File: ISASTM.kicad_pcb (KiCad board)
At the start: 4 copper layers, 101.6 x 101.6 mm, 137 parts, among them J1 Bus_ISA_8bit, J2 USB_C_Receptacle_USB2.0, J3 Boot select, J4 USB_C_Receptacle_USB2.0, J5 TagConnect_TC2030_SWD, SW1 Reset, U1 STM32H743IITx, U10 SN74AVC8T245PW, U11 SN74AVC8T245PW, U12 SN74AVC8T245PW, U13 SN74AVC8T245PW, U14 SRV05-4, U15 USB3343, U2 MT48LC16M16A2P, U3 SN74AVC8T245PW, U4 SN74AVC8T245PW, U5 AMS1117-3.3, U6 SN74AVC8T245PW, U7 SN74AVC8T245PW, U8 SN74AVC8T245PW, U9 SN74AVC8T245PW, X1 SG-7050CAN, Y1 26 MHz, Y2 8 MHz

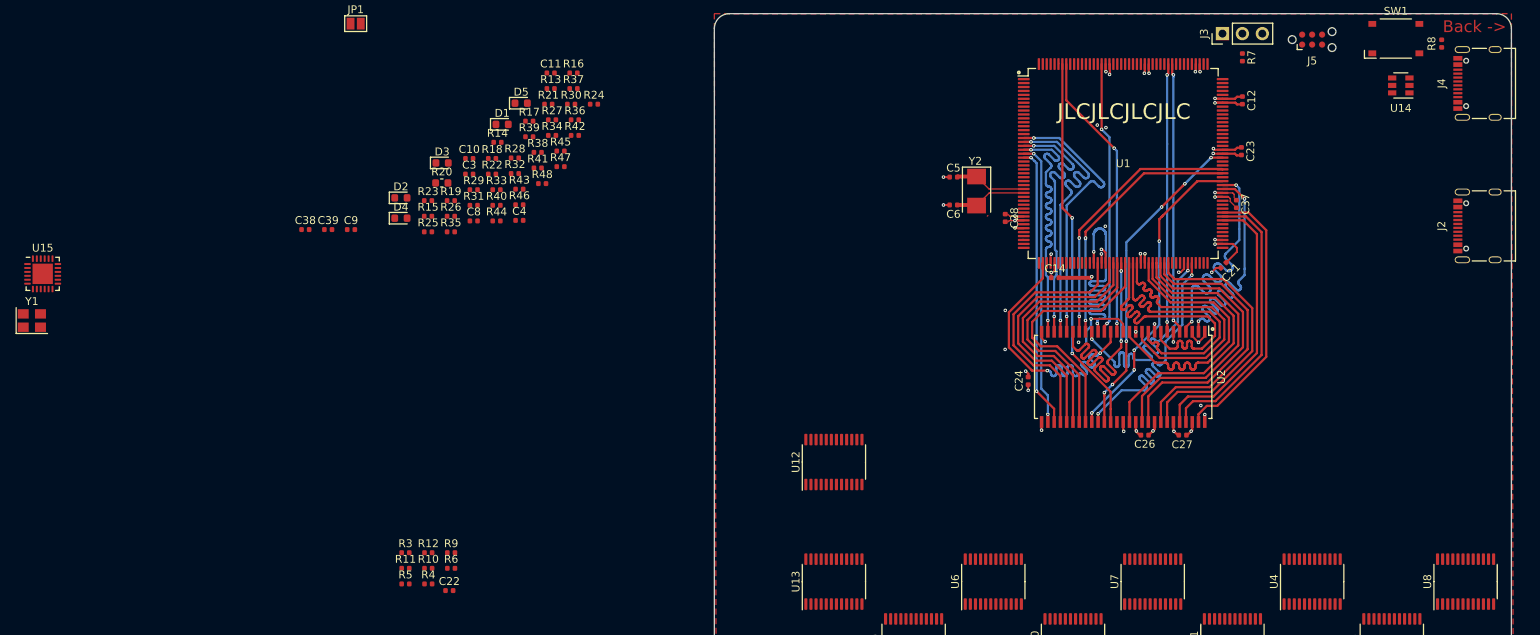
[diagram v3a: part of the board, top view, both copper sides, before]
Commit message: Finish fanout and ULPI routing
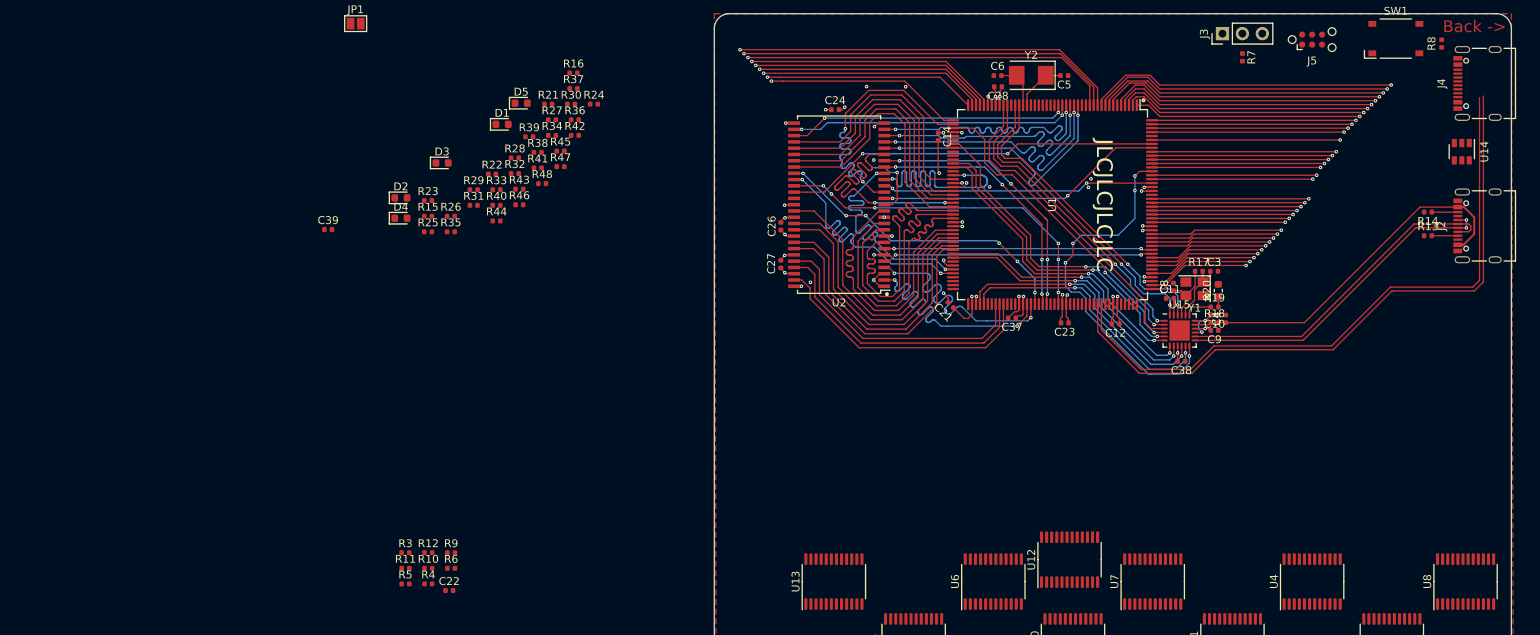
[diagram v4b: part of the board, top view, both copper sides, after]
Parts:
- moved Y1 148.3 mm to (76.5, 49.7), turned to 180 degrees
- moved U15 145.1 mm to (74.5, 55.0)
- moved R14 118.9 mm to (106.2, 39.9), turned to 180 degrees
- moved R13 113.4 mm to (106.2, 42.9)
- moved C38 112.9 mm to (74.8, 58.9), turned to 180 degrees
- moved C9 110.8 mm to (79.0, 55.0), turned to 180 degrees
- moved R20 99.9 mm to (79.5, 49.9), turned to 90 degrees
- moved R19 98.3 mm to (79.0, 52.0)
- moved C10 97.1 mm to (79.0, 53.0), turned to 180 degrees
- moved C3 95.8 mm to (79.0, 47.4)
- moved R18 94.4 mm to (79.0, 54.0)
- moved C4 90.9 mm to (80.4, 53.5), turned to 90 degrees
- moved C8 89.6 mm to (73.8, 49.4), turned to 90 degrees
- moved R17 87.5 mm to (77.0, 47.4)
- moved C11 84.0 mm to (73.3, 50.9)
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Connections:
- net Net-(J2-PadA6) renamed /USB_HS+
- net Net-(J2-PadA7) renamed /USB_HS-
- U1 pad 1: Net-(U1-Pad1) -> /LV_A0
- U1 pad 107: Net-(U1-Pad107) -> /LV_CLK
- U1 pad 110: Net-(U1-Pad110) -> /~LV_IO_CH_CK
- U1 pad 111: Net-(U1-Pad111) -> /LV_IO_CH_RDY
- U1 pad 2: Net-(U1-Pad2) -> /LV_A1
- U1 pad 29: Net-(C6-Pad1) -> Net-(C5-Pad2)
- U1 pad 3: Net-(U1-Pad3) -> /LV_A2
- U1 pad 30: Net-(C5-Pad2) -> Net-(C6-Pad1)
- U1 pad 4: Net-(U1-Pad4) -> /LV_A3
- U1 pad 43: Net-(U1-Pad43) -> /~LV_DACK2
- U1 pad 44: Net-(U1-Pad44) -> /~LV_DACK1
- U1 pad 45: Net-(U1-Pad45) -> /LV_TC
- U1 pad 5: Net-(U1-Pad5) -> /LV_A4
- U1 pad 52: /~LV_DACK1 -> Net-(U1-Pad52)
- U1 pad 53: /~LV_DACK2 -> Net-(U1-Pad53)
- U1 pad 54: /LV_TC -> Net-(U1-Pad54)
- U1 pad 55: /LV_CLK -> Net-(U1-Pad55)
- U1 pad 58: /LV_IO_CH_RDY -> Net-(U1-Pad58)
- U1 pad 85: /LV_A0 -> Net-(U1-Pad85)
- U1 pad 86: /LV_A1 -> Net-(U1-Pad86)
- U1 pad 87: /LV_A2 -> Net-(U1-Pad87)
- U1 pad 88: /LV_A3 -> Net-(U1-Pad88)
- U1 pad 89: /LV_A4 -> Net-(U1-Pad89)
- U1 pad 94: /~LV_IO_CH_CK -> Net-(U1-Pad94)
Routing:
- net /USB_FS_D-: track 0.00 -> 83.4 mm
- net /USB_FS_D+: track 0.00 -> 81.6 mm
- net /LV_A17: track 0.00 -> 49.8 mm, vias 0 -> 1
- net /LV_A18: track 0.00 -> 48.7 mm, vias 0 -> 1
- net /LV_A19: track 0.00 -> 47.6 mm, vias 0 -> 1
- net /OTG_HS_ULPI_D7: track 0.00 -> 47.1 mm, vias 0 -> 5
- net Net-(C4-Pad1): track 0.00 -> 44.1 mm
- net /USB_HS-: track 0.00 -> 43.4 mm
- net /USB_HS+: track 0.00 -> 42.7 mm, vias 0 -> 2
- net /OTG_HS_ULPI_D0: track 0.00 -> 40.6 mm, vias 0 -> 2
- net /OTG_HS_ULPI_NXT: track 0.00 -> 40.6 mm
- net /OTG_HS_ULPI_CK: track 0.00 -> 40.3 mm, vias 0 -> 2
- net /~RESET: track 0.00 -> 40.2 mm, vias 0 -> 2
- net /OTG_HS_ULPI_D1: track 0.00 -> 40.1 mm, vias 0 -> 2
- net /OTG_HS_ULPI_D2: track 0.00 -> 39.7 mm, vias 0 -> 2
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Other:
- rule trace_min: 0.127 -> 0.09

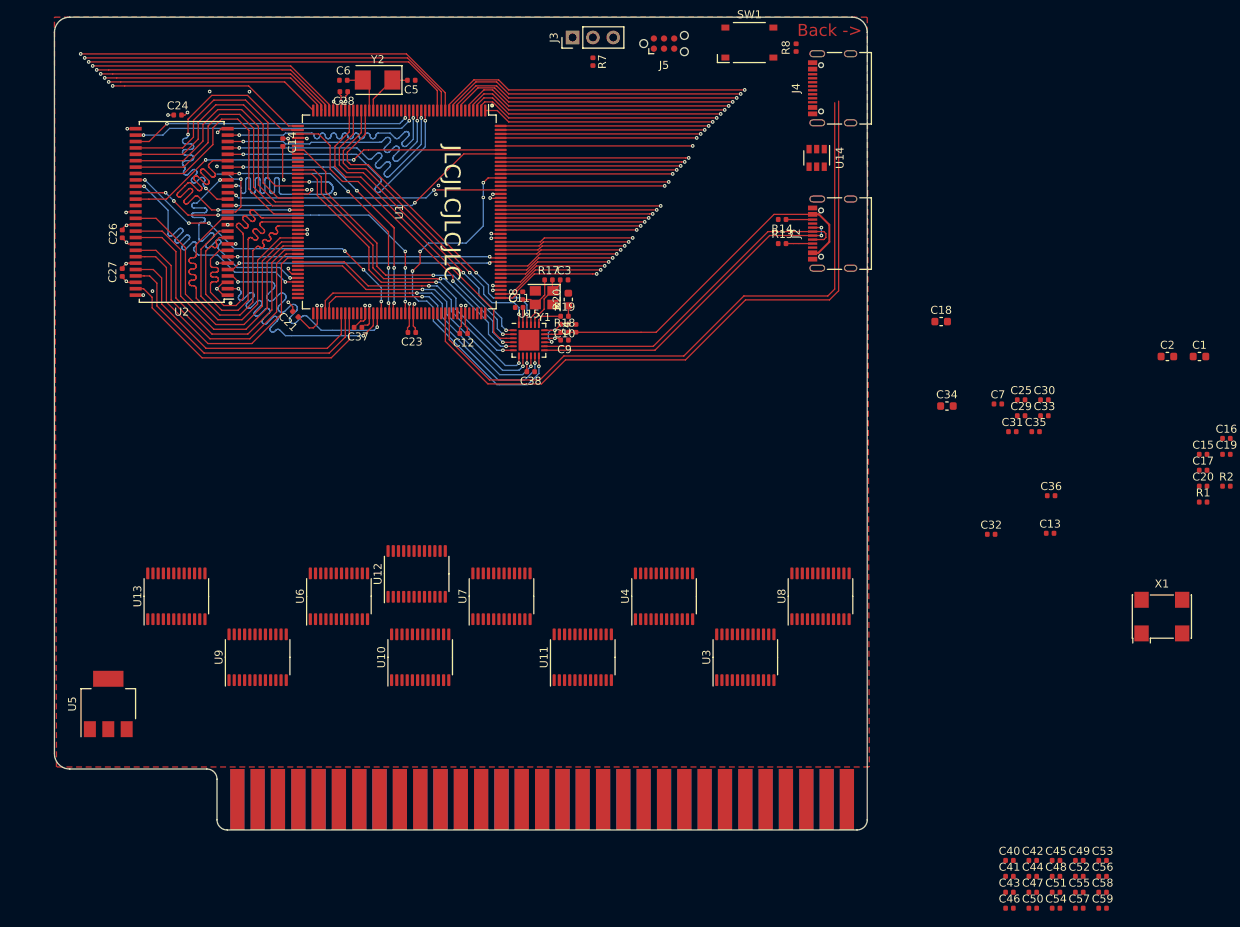
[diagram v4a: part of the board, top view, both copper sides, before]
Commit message: Partial ISA bus layout
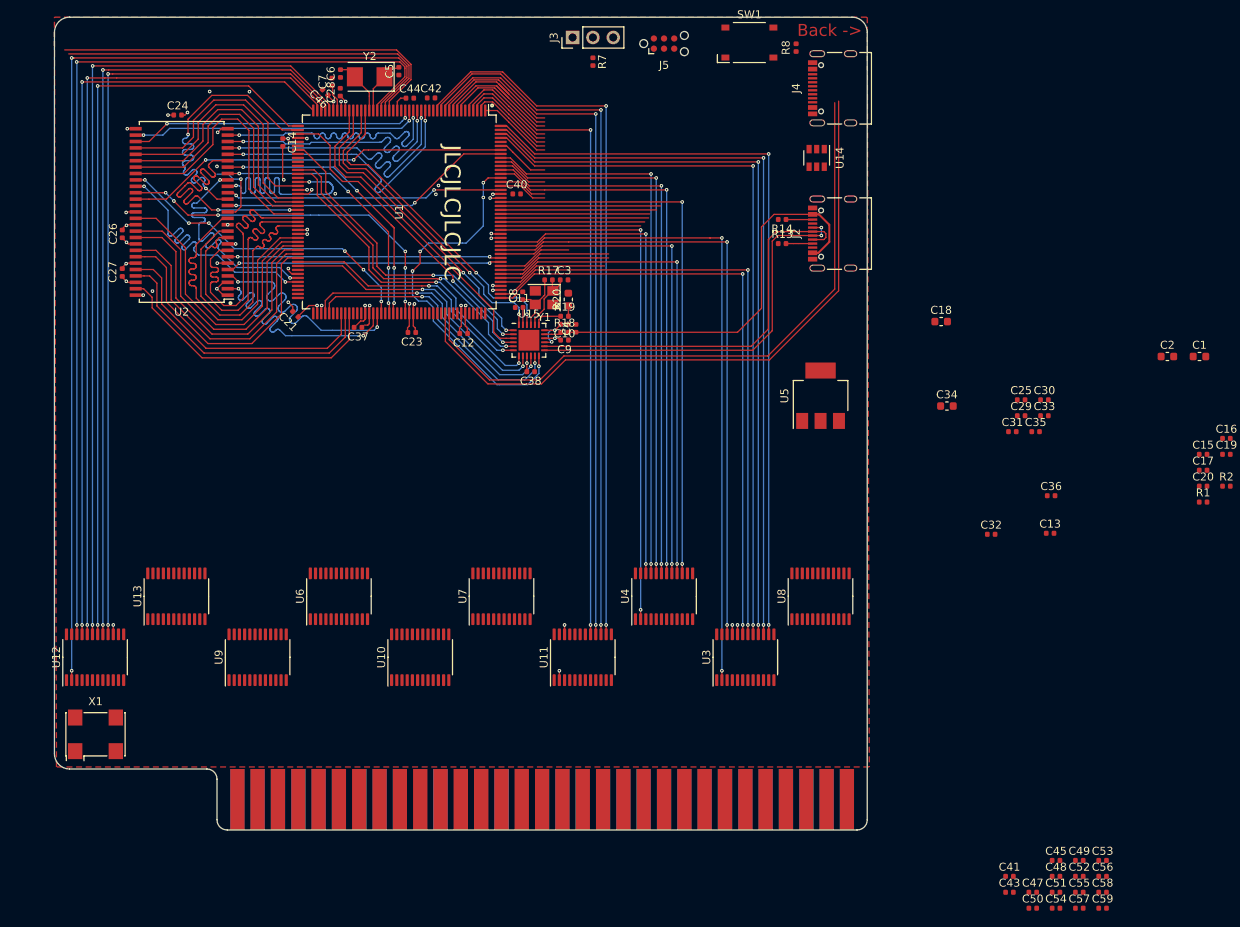
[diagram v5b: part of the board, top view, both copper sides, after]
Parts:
- moved X1 134.1 mm to (20.4, 104.3)
- moved C46 133.1 mm to (49.1, 24.0), turned to 135 degrees
- moved C44 124.6 mm to (59.7, 24.7)
- moved C42 121.4 mm to (62.3, 24.7)
- moved C40 103.6 mm to (73.0, 36.7)
- moved U5 97.0 mm to (111.0, 61.9)
- moved C7 92.4 mm to (49.9, 22.7), turned to 90 degrees
- moved U12 41.5 mm to (20.3, 94.6)
- moved C5 1.93 mm to (58.3, 21.4), turned to 90 degrees
- moved Y2 1.07 mm to (54.6, 22.1)
- moved C6 0.91 mm to (51.0, 21.7), turned to 270 degrees
- moved C28 0.44 mm to (51.0, 24.0), turned to 90 degrees
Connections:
- U1 pad 107: /LV_CLK -> /LV_DRQ2
- U1 pad 115: /~LV_NOWS -> /LV_DRQ3
- U1 pad 119: /~LV_DACK3 -> /LV_DRQ1
- U1 pad 120: /LV_AEN -> /LV_IRQ2
- U1 pad 121: /LV_ALE -> Net-(U1-Pad121)
- U1 pad 138: Net-(U1-Pad138) -> /LV_ALE
- U1 pad 144: /LV_IRQ2 -> /LV_AEN
- U1 pad 145: /LV_IRQ3 -> /~DATA_OE
- U1 pad 146: /LV_IRQ4 -> /DATA_DIR
- U1 pad 147: /LV_IRQ5 -> /~CONTROL1_OE
- U1 pad 150: /LV_IRQ6 -> /CONTROL1_DIR
- U1 pad 157: Net-(U1-Pad157) -> /LV_ISARESET
- U1 pad 24: Net-(U1-Pad24) -> /LV_IRQ5
- U1 pad 25: Net-(U1-Pad25) -> /LV_IRQ4
- U1 pad 26: Net-(U1-Pad26) -> /LV_IRQ3
- U1 pad 27: Net-(U1-Pad27) -> /CONTROL3_DIR
- U1 pad 28: Net-(U1-Pad28) -> /~CONTROL3_OE
- U1 pad 40: /LV_DRQ1 -> /~LV_DACK3
- U1 pad 41: /LV_DRQ2 -> /LV_CLK
- U1 pad 42: /LV_DRQ3 -> /~LV_NOWS
- U1 pad 50: /LV_ISARESET -> Net-(U1-Pad50)
- U1 pad 89: Net-(U1-Pad89) -> /LV_IRQ6
- U11 pad 10: GND -> /A19
- U11 pad 14: GND -> /LV_A19
- U11 pad 15: GND -> /LV_A18
- U11 pad 16: GND -> /LV_A17
- U11 pad 17: GND -> /LV_A16
- U11 pad 18: /LV_A19 -> GND
- U11 pad 19: /LV_A18 -> GND
- U11 pad 20: /LV_A17 -> GND
- U11 pad 21: /LV_A16 -> GND
- U11 pad 3: /A16 -> GND
- U11 pad 4: /A17 -> GND
- U11 pad 5: /A18 -> GND
- U11 pad 6: /A19 -> GND
- U11 pad 7: GND -> /A16
- U11 pad 8: GND -> /A17
- U11 pad 9: GND -> /A18
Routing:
- net /CONTROL3_DIR: track 0.00 -> 127.2 mm, vias 0 -> 2
- net /~CONTROL3_OE: track 0.00 -> 119.7 mm, vias 0 -> 2
- net /~LV_DACK3: track 0.00 -> 103.4 mm, vias 0 -> 2
- net /LV_CLK: track 0.00 -> 100.9 mm, vias 0 -> 2
- net /~LV_NOWS: track 0.00 -> 99.2 mm, vias 0 -> 2
- net /DATA_DIR: track 0.00 -> 83.3 mm, vias 0 -> 2
- net /~DATA_OE: track 0.00 -> 77.7 mm, vias 0 -> 2
- net /~LV_DACK1: track 27.1 -> 99.4 mm, vias 1 -> 2
- net /~LV_DACK2: track 28.7 -> 100.4 mm, vias 1 -> 2
- net /LV_TC: track 25.2 -> 95.6 mm, vias 1 -> 2
- net /LV_ISARESET: track 0.00 -> 69.1 mm, vias 0 -> 2
- net /LV_D7: track 26.0 -> 95.0 mm, vias 1 -> 2
- net /LV_D6: track 25.5 -> 93.8 mm, vias 1 -> 2
- net /LV_D5: track 25.0 -> 92.7 mm, vias 1 -> 2
- net /LV_D4: track 24.5 -> 91.6 mm, vias 1 -> 2
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
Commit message: Route LV bus
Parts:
- moved C21 3.15 mm to (47.7, 53.9), turned to 225 degrees
- moved C37 1.38 mm to (54.1, 54.4), turned to 270 degrees
- moved C23 0.61 mm to (59.3, 53.8), turned to 270 degrees
- moved C12 0.33 mm to (66.5, 53.8), turned to 270 degrees
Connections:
- U1 pad 100: Net-(U1-Pad100) -> /LV_IRQ5
- U1 pad 101: Net-(U1-Pad101) -> /LV_IRQ6
- U1 pad 115: /LV_DRQ3 -> /LV_A6
- U1 pad 116: Net-(U1-Pad116) -> /LV_A7
- U1 pad 121: Net-(U1-Pad121) -> /LV_DRQ3
- U1 pad 128: /LV_A5 -> /~IRQ_OE
- U1 pad 129: /LV_A6 -> /ADDRESS_DIR
- U1 pad 130: /LV_A7 -> /~ADDRESS_OE
- U1 pad 24: /LV_IRQ5 -> /IRQ_DIR
- U1 pad 25: /LV_IRQ4 -> /SPARE2_DIR
- U1 pad 26: /LV_IRQ3 -> /~SPARE2_OE
- U1 pad 55: Net-(U1-Pad55) -> /LV_A5
- U1 pad 85: Net-(U1-Pad85) -> /~SPARE1_OE
- U1 pad 88: Net-(U1-Pad88) -> /CONTROL2_DIR
- U1 pad 89: /LV_IRQ6 -> /~CONTROL2_OE
- U1 pad 94: Net-(U1-Pad94) -> /SPARE1_DIR
- U1 pad 95: Net-(U1-Pad95) -> /LV_IRQ3
- U1 pad 99: Net-(U1-Pad99) -> /LV_IRQ4
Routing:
- net /IRQ_DIR: track 0.00 -> 153.4 mm, vias 0 -> 4
- net /LV_A0: track 9.47 -> 149.1 mm, vias 0 -> 4
- net /LV_A1: track 11.0 -> 149.5 mm, vias 0 -> 4
- net /LV_A2: track 11.8 -> 149.2 mm, vias 0 -> 4
- net /LV_A3: track 12.5 -> 148.8 mm, vias 0 -> 4
- net /LV_A4: track 13.2 -> 148.3 mm, vias 0 -> 4
- net /SPARE2_DIR: track 0.00 -> 132.6 mm, vias 0 -> 2
- net /~SPARE2_OE: track 0.00 -> 130.2 mm, vias 0 -> 2
- net /SPARE1_DIR: track 0.00 -> 100.4 mm, vias 0 -> 4
- net /LV_A15: track 15.9 -> 115.6 mm, vias 0 -> 4
- net /~SPARE1_OE: track 0.00 -> 97.1 mm, vias 0 -> 4
- net /LV_A13: track 16.8 -> 113.9 mm, vias 0 -> 4
- net /ADDRESS_DIR: track 1.18 -> 97.5 mm, vias 1 -> 2
- net /LV_A14: track 19.0 -> 113.8 mm, vias 0 -> 4
- net /~ADDRESS_OE: track 1.18 -> 93.3 mm, vias 1 -> 2
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
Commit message: Place bias resistors
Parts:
- moved R36 138.7 mm to (114.8, 102.1), turned to 180 degrees
- moved R29 137.8 mm to (105.4, 103.4)
- moved R11 134.9 mm to (109.7, 102.1)
- moved R12 134.8 mm to (112.3, 102.1)
- moved C22 134.1 mm to (113.8, 66.3)
- moved R27 129.8 mm to (100.3, 103.4)
- moved R10 129.5 mm to (107.2, 102.1)
- moved C50 126.0 mm to (16.8, 90.1), turned to 180 degrees
- moved R35 125.4 mm to (91.9, 102.1), turned to 180 degrees
- moved R5 124.5 mm to (99.5, 102.1)
- moved R9 124.3 mm to (104.6, 102.1)
- moved C52 123.7 mm to (25.6, 84.3), turned to 270 degrees
- moved R6 121.6 mm to (102.1, 102.1)
- moved R47 120.6 mm to (106.1, 82.6), turned to 90 degrees
- moved R3 120.1 mm to (94.5, 102.1)
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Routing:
- net /SWDIO: track 9.67 -> 53.1 mm, vias 0 -> 3
- net /LED1: track 18.0 -> 55.1 mm
- net /LED2: track 18.5 -> 54.1 mm
- net /LED3: track 18.6 -> 53.4 mm
- net /LED4: track 19.5 -> 52.0 mm
- net /LED5: track 20.0 -> 51.1 mm
- net Net-(C1-Pad1): track 0.00 -> 18.0 mm, vias 0 -> 2
- net Net-(C2-Pad2): track 0.00 -> 15.2 mm, vias 0 -> 2
- net Net-(R1-Pad1): track 6.84 -> 21.5 mm
- net /D6: track 0.00 -> 10.8 mm
- net /D3: track 0.00 -> 10.7 mm
- net /D2: track 0.00 -> 10.7 mm
- net /~IO_CH_CK: track 0.00 -> 10.5 mm
- net /D5: track 0.00 -> 10.5 mm
- net /D4: track 0.00 -> 10.4 mm
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
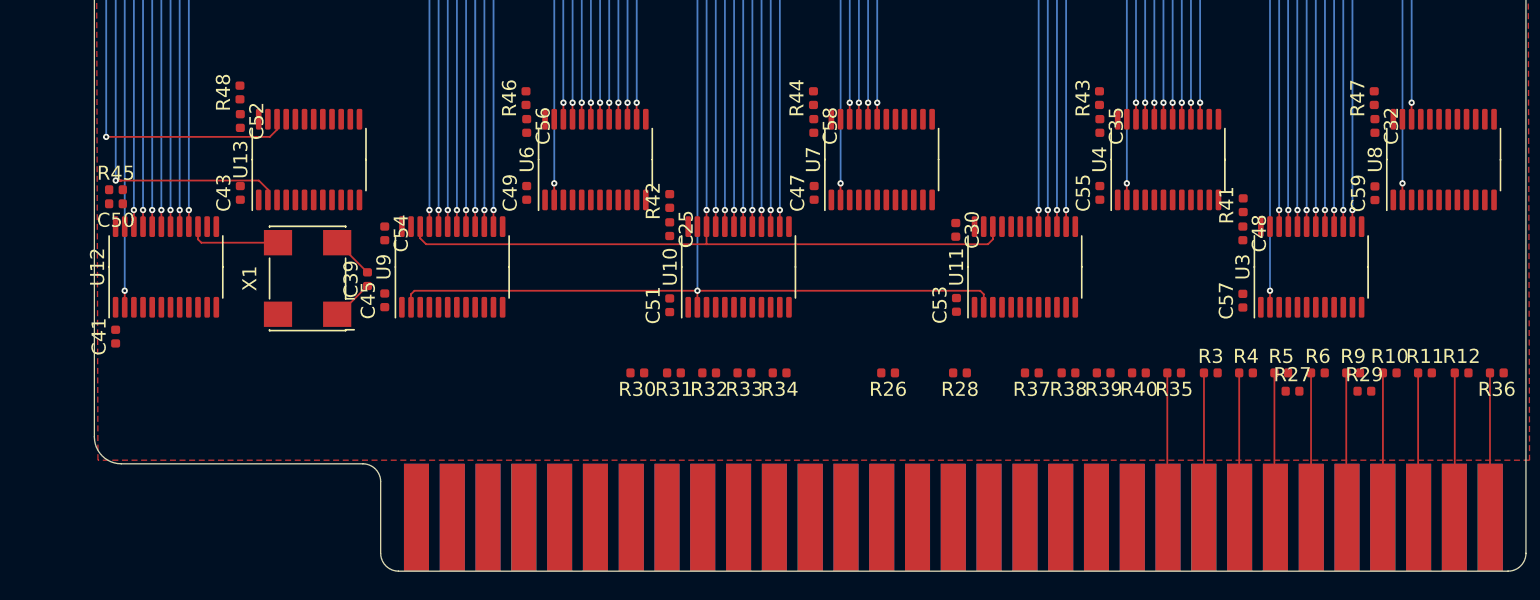
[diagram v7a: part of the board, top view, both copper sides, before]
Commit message: Hook up ISA address + data
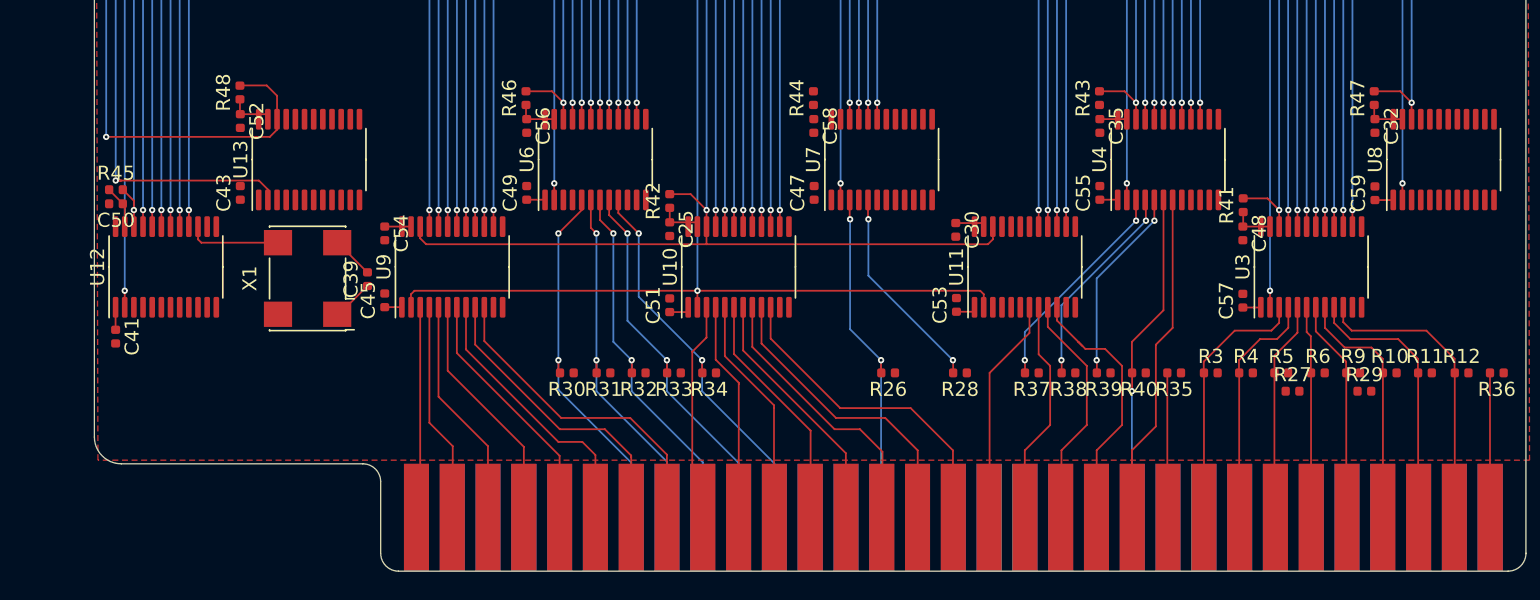
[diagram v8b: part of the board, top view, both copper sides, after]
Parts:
- moved R30 5.00 mm to (48.8, 102.1)
- moved R31 5.00 mm to (51.4, 102.1)
- moved R32 5.00 mm to (53.9, 102.1)
- moved R33 5.00 mm to (56.4, 102.1)
- moved R34 5.00 mm to (58.9, 102.1)
- turned C41 to 270 degrees
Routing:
- net /IRQ7: track 0.00 -> 27.9 mm, vias 0 -> 2
- net /IRQ6: track 0.00 -> 27.1 mm, vias 0 -> 2
- net /IRQ5: track 0.00 -> 26.5 mm, vias 0 -> 2
- net /IRQ3: track 0.00 -> 26.2 mm, vias 0 -> 2
- net /IRQ4: track 0.00 -> 25.7 mm, vias 0 -> 2
- net /DRQ1: track 0.00 -> 24.4 mm, vias 0 -> 2
- net /AEN: track 0.00 -> 23.8 mm
- net /~SMEMW: track 0.00 -> 23.4 mm, vias 0 -> 1
- net /A15: track 0.00 -> 23.1 mm
- net +3V3: track 53.8 -> 76.9 mm
- net /A7: track 0.00 -> 23.1 mm
- net /A14: track 0.00 -> 21.6 mm
- net /A6: track 0.00 -> 21.4 mm
- net /A13: track 0.00 -> 19.7 mm
- net /A5: track 0.00 -> 19.7 mm
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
